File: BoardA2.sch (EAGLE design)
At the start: 9 parts, among them J1 FEMALE 2x3

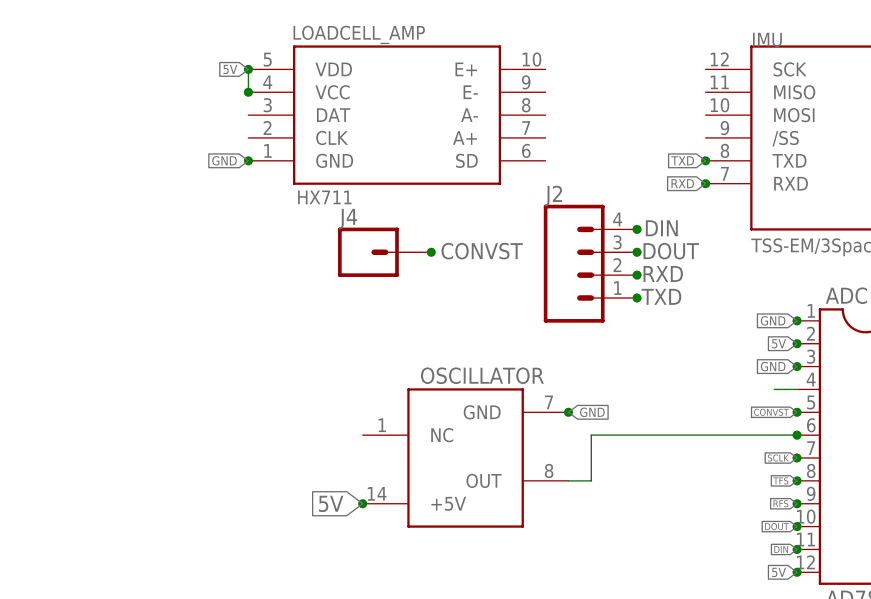
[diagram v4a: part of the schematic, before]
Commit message: Updated
Fixed Hole placment,connectors, routing issues
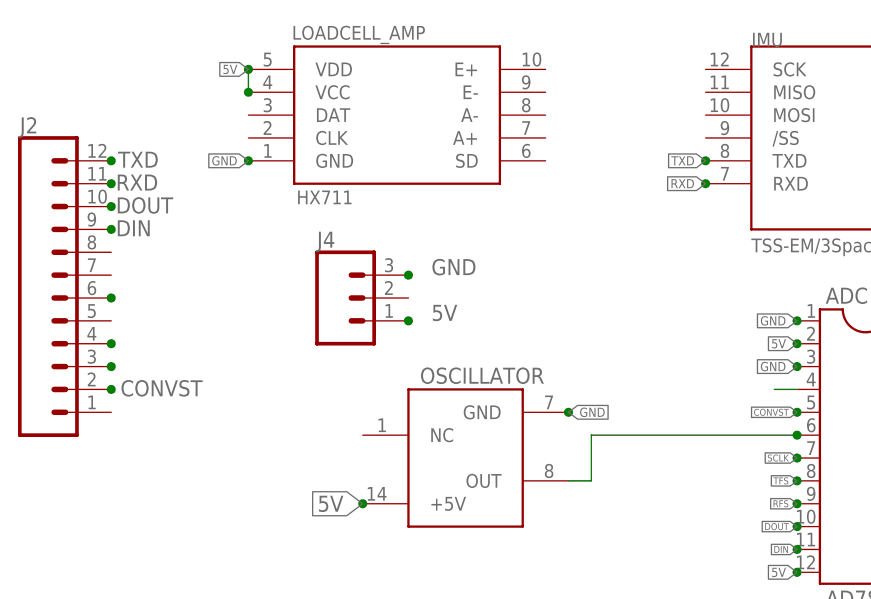
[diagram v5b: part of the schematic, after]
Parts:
- J2: device SparkFun-Connectors:CONN_04 -> SparkFun-Connectors:CONN_12
- J4: device SparkFun-Connectors:CONN_01 -> SparkFun-Connectors:CONN_03
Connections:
- new net N$5: J2.6
- net 5V: now also J4.2
- net CONVST: no longer J4.1
- net DIN: now also J2.1; no longer J2.4
- net DOUT: now also J2.2; no longer J2.3
- net GND: now also J4.3
- net RXD: now also J2.3; no longer J2.2
- net TXD: now also J2.4; no longer J2.1
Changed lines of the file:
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@@
 <part name="IMU" library="Smartcrutches" deviceset="IMU" device="" value="TSS-EM/3Space"/>
 <part name="LOADCELL_AMP" library="Smartcrutches" deviceset="LOADCELLAMP" device="" value="HX711"/>
-<part name="J2" library="SparkFun-Connectors" deviceset="CONN_04" device=""/>
+<part name="J2" library="SparkFun-Connectors" deviceset="CONN_12" device=""/>
 <part name="J3" library="SparkFun-Connectors" deviceset="CONN_04" device=""/>
-<part name="J4" library="SparkFun-Connectors" deviceset="CONN_01" device=""/>
+<part name="J4" library="SparkFun-Connectors" deviceset="CONN_03" device=""/>
 </parts>
 <sheets>
@@
 <instance part="IMU" gate="G$1" x="-7.62" y="83.82"/>
 <instance part="LOADCELL_AMP" gate="G$1" x="-55.88" y="86.36"/>
-<instance part="J2" gate="G$1" x="-35.56" y="68.58"/>
+<instance part="J2" gate="G$1" x="-99.06" y="68.58"/>
 <instance part="J3" gate="G$1" x="25.4" y="86.36"/>
-<instance part="J4" gate="G$1" x="-60.96" y="71.12"/>
+<instance part="J4" gate="J$1" x="-63.5" y="66.04"/>
 </instances>
 <busses>
@@
 <wire x1="-73.66" y1="91.44" x2="-73.66" y2="88.9" width="0.1524" layer="91"/>
 </segment>
+<segment>
+<pinref part="J4" gate="J$1" pin="2"/>
+<junction x="-55.88" y="63.5"/>
+<label x="-53.34" y="63.5" size="1.778" layer="95"/>
+</segment>
 </net>
 <net name="N$1" class="0">
@@
 <label x="-73.66" y="81.28" size="1.016" layer="95" rot="R180" xref="yes"/>
 </segment>
+<segment>
+<pinref part="J4" gate="J$1" pin="3"/>
+<junction x="-55.88" y="68.58"/>
+<label x="-53.34" y="68.58" size="1.778" layer="95"/>
+</segment>
 </net>
 <net name="N$4" class="0">
@@
 </segment>
 <segment>
-<pinref part="J2" gate="G$1" pin="4"/>
-<junction x="-30.48" y="73.66"/>
-<label x="-29.718" y="72.898" size="1.778" layer="95"/>
+<pinref part="J2" gate="G$1" pin="1"/>
+<junction x="-88.9" y="73.66"/>
+<label x="-88.392" y="72.898" size="1.778" layer="95"/>
 </segment>
 </net>
@@
 </segment>
 <segment>
-<pinref part="J2" gate="G$1" pin="3"/>
-<junction x="-30.48" y="71.12"/>
-<label x="-29.972" y="70.358" size="1.778" layer="95"/>
+<pinref part="J2" gate="G$1" pin="2"/>
+<junction x="-88.9" y="76.2"/>
+<label x="-88.392" y="75.438" size="1.778" layer="95"/>
 </segment>
 </net>
@@
 </segment>
 <segment>
-<pinref part="J4" gate="G$1" pin="1"/>
-<junction x="-53.34" y="71.12"/>
-<label x="-52.324" y="70.358" size="1.778" layer="95"/>
+<junction x="-88.9" y="55.88"/>
+<label x="-87.884" y="55.118" size="1.778" layer="95"/>
 </segment>
 </net>
@@
 </segment>
 <segment>
-<pinref part="J2" gate="G$1" pin="1"/>
-<junction x="-30.48" y="66.04"/>
-<label x="-29.972" y="65.278" size="1.778" layer="95"/>
+<pinref part="J2" gate="G$1" pin="4"/>
+<junction x="-88.9" y="81.28"/>
+<label x="-88.138" y="80.518" size="1.778" layer="95"/>
+<junction x="-88.9" y="60.96"/>
 </segment>
 </net>
@@
 </segment>
 <segment>
-<pinref part="J2" gate="G$1" pin="2"/>
-<junction x="-30.48" y="68.58"/>
-<label x="-29.972" y="67.818" size="1.778" layer="95"/>
+<pinref part="J2" gate="G$1" pin="3"/>
+<junction x="-88.9" y="78.74"/>
+<label x="-88.392" y="77.978" size="1.778" layer="95"/>
+<junction x="-88.9" y="58.42"/>
 </segment>
 </net>
@@
 </segment>
 </net>
+<net name="N$5" class="0">
+<segment>
+<pinref part="J2" gate="G$1" pin="6"/>
+<junction x="-88.9" y="66.04"/>
+</segment>
+</net>

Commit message: Motor Components
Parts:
- added D1: 1N4004, diode:1N4004
- added Q1: 2N2222, transistor-npn:2N2222
- added R1, R2: (no value), eagle-ltspice:R0204/7
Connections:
- new net MOTOR: R1.2
- new net N$7: Q1.B, R1.1, R2.1
- net GND: now also Q1.E, R2.2
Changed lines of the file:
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@@
 <part name="J3" library="SparkFun-Connectors" deviceset="CONN_04" device=""/>
 <part name="J4" library="SparkFun-Connectors" deviceset="CONN_03" device=""/>
+<part name="D1" library="diode" library_urn="urn:adsk.eagle:library:210" deviceset="1N4004" device=""/>
+<part name="Q1" library="transistor-npn" library_urn="urn:adsk.eagle:library:398" deviceset="2N2222*" device=""/>
+<part name="R1" library="eagle-ltspice" library_urn="urn:adsk.eagle:library:217" deviceset="R" device="0204/7"/>
+<part name="R2" library="eagle-ltspice" library_urn="urn:adsk.eagle:library:217" deviceset="R" device="0204/7"/>
 </parts>
 <sheets>
@@
 <instance part="J3" gate="G$1" x="25.4" y="86.36"/>
 <instance part="J4" gate="J$1" x="-63.5" y="66.04"/>
+<instance part="D1" gate="1" x="-78.74" y="25.4" rot="R90"/>
+<instance part="Q1" gate="G$1" x="-88.9" y="27.94"/>
+<instance part="R1" gate="G$1" x="-101.6" y="27.94" rot="R180"/>
+<instance part="R2" gate="G$1" x="-91.44" y="17.78"/>
 </instances>
 <busses>
@@
 <label x="-53.34" y="68.58" size="1.778" layer="95"/>
 </segment>
+<segment>
+<pinref part="R2" gate="G$1" pin="2"/>
+<pinref part="Q1" gate="G$1" pin="E"/>
+<wire x1="-86.36" y1="17.78" x2="-86.36" y2="22.86" width="0.1524" layer="91"/>
+<junction x="-86.36" y="22.86"/>
+<junction x="-86.36" y="17.78"/>
+<label x="-86.36" y="17.78" size="1.778" layer="95" rot="R270" xref="yes"/>
+</segment>
 </net>
 <net name="N$4" class="0">
@@
 </segment>
 </net>
+<net name="N$7" class="0">
+<segment>
+<pinref part="Q1" gate="G$1" pin="B"/>
+<pinref part="R1" gate="G$1" pin="1"/>
+<wire x1="-91.44" y1="27.94" x2="-96.52" y2="27.94" width="0.1524" layer="91"/>
+<pinref part="R2" gate="G$1" pin="1"/>
+<wire x1="-96.52" y1="17.78" x2="-96.52" y2="27.94" width="0.1524" layer="91"/>
+<junction x="-91.44" y="27.94"/>
+<junction x="-96.52" y="27.94"/>
+</segment>
+</net>
+<net name="MOTOR" class="0">
+<segment>
+<pinref part="R1" gate="G$1" pin="2"/>
+<junction x="-106.68" y="27.94"/>
+<label x="-106.68" y="27.94" size="1.778" layer="95" rot="R180" xref="yes"/>
+</segment>
+</net>

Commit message: update-moved capacitor
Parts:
- added J5: (no value), SparkFun-Connectors:CONN_05
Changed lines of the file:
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@@
 <part name="R1" library="eagle-ltspice" library_urn="urn:adsk.eagle:library:217" deviceset="R" device="0204/7"/>
 <part name="R2" library="eagle-ltspice" library_urn="urn:adsk.eagle:library:217" deviceset="R" device="0204/7"/>
+<part name="J5" library="SparkFun-Connectors" deviceset="CONN_05" device=""/>
 </parts>
 <sheets>
@@
 <instance part="R1" gate="G$1" x="-101.6" y="27.94" rot="R180"/>
 <instance part="R2" gate="G$1" x="-91.44" y="17.78"/>
+<instance part="J5" gate="G$1" x="38.1" y="35.56"/>
 </instances>
 <busses>
